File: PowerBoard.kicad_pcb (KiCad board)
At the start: 4 copper layers, 100 x 100 mm, 30 parts, among them U1 LT8342RV-TRMPBF, U11 PINA745AIRELR, U2 AD5259BRMZ100

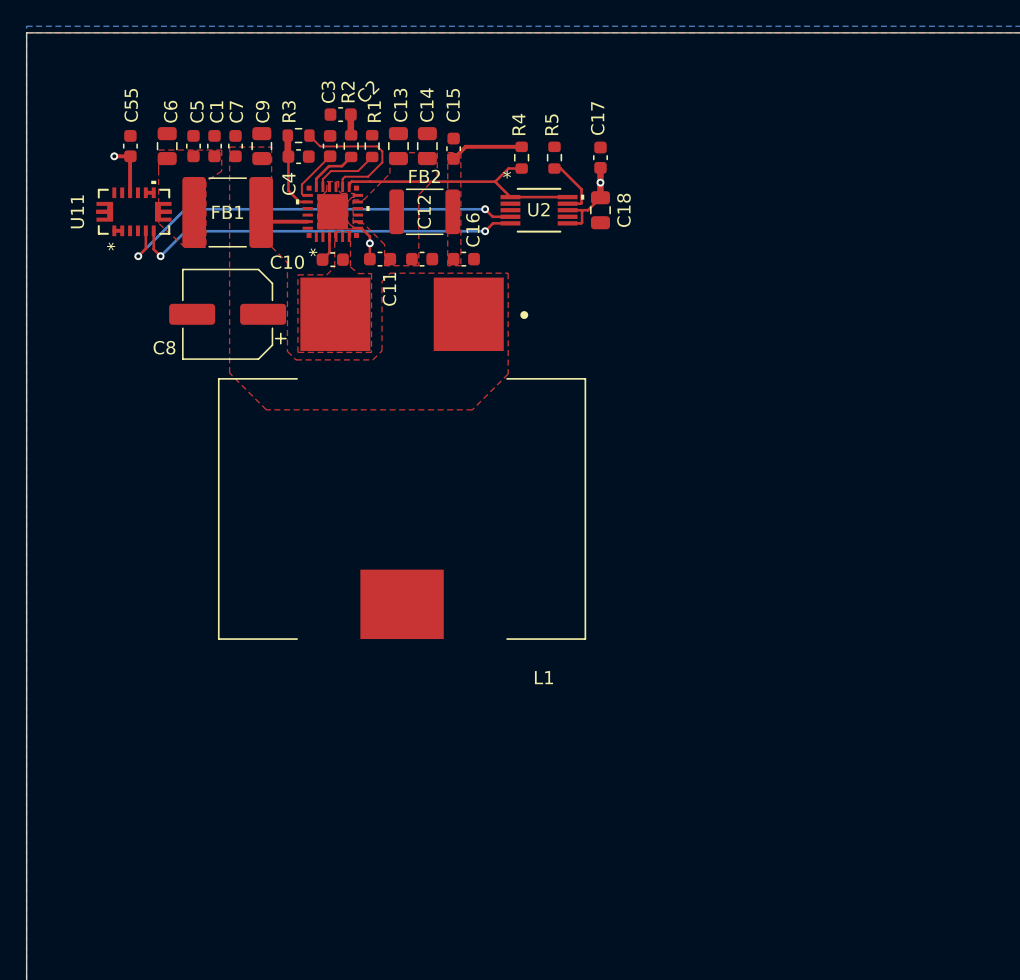
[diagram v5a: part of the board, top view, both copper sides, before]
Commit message: Most of frontend layout done. Still need to add in power and analog ground
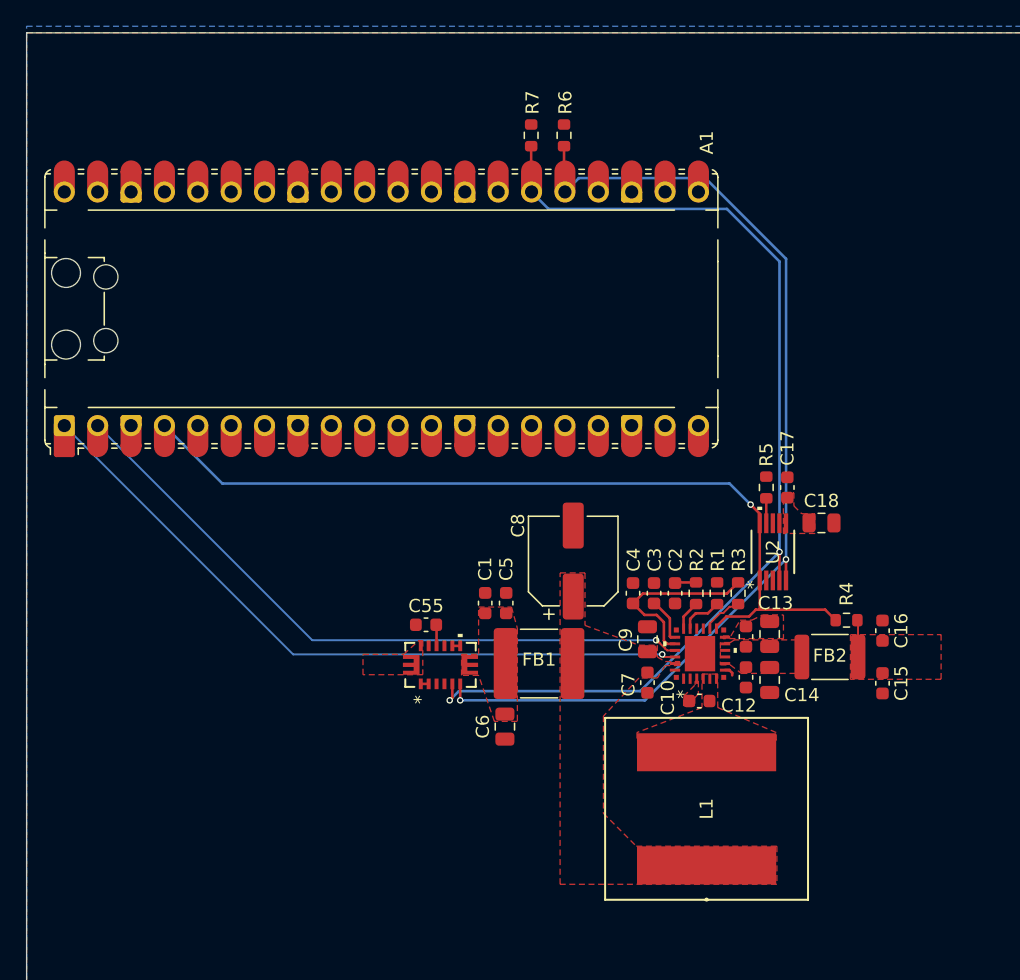
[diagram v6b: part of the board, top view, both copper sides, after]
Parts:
- added A1: RaspberryPi_Pico, Module:RaspberryPi_Pico_Common_Unspecified, F.Cu at (122.0, 65.5)
- added R6: 33k, Resistor_SMD:R_0603_1608Metric, F.Cu at (133.4, 52.3)
- added R7: 33k, Resistor_SMD:R_0603_1608Metric, F.Cu at (135.9, 52.3)
- L1: footprint _PowerBoard:IND_SER2918H-333KL -> _PowerBoard:IND_XGL1313_COC
- moved C15 52.2 mm to (160.1, 94.0), turned to -90 degrees
- moved C7 51.5 mm to (142.2, 94.0), turned to 90 degrees
- moved C6 51.1 mm to (131.4, 97.3), turned to 90 degrees
- moved R3 48.3 mm to (149.2, 87.2), turned to -90 degrees
- moved C14 48.3 mm to (151.6, 93.8), turned to 90 degrees
- moved C9 47.6 mm to (142.2, 90.7)
- moved C13 46.7 mm to (151.6, 90.2)
- moved FB2 45.8 mm to (156.1, 92.0)
- moved C2 44.4 mm to (144.3, 87.2), turned to 90 degrees
- moved U1 43.7 mm to (146.2, 91.8)
- moved C10 43.7 mm to (146.2, 95.3)
- moved R4 43.0 mm to (157.4, 89.2), turned to 0 degrees
- moved R1 43.0 mm to (147.6, 87.2)
- moved R2 43.0 mm to (145.9, 87.2)
- moved C55 42.8 mm to (125.4, 89.5), turned to 0 degrees
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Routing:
- net /Main/SX_B.EN: track 0.00 -> 53.8 mm, vias 0 -> 1
- net /Main/SX_B.PGOOD: track 0.00 -> 51.0 mm, vias 0 -> 1
- net /Main/SCL: track 29.7 -> 77.6 mm
- net /Main/SDA: track 32.2 -> 79.2 mm
- net /Main/SX_B.FB: track 20.5 -> 65.5 mm, vias 0 -> 1
- net +5V: track 11.2 -> 1.76 mm, vias 2 -> 0
- net Net-(U1-VSET1): track 11.0 -> 3.08 mm
- net /Main/boost_a_frontend/INTVCC: track 6.04 -> 14.0 mm
- net Net-(U1-VIN): track 3.83 -> 0.00 mm
- net Net-(U2-B): track 4.84 -> 1.90 mm
- net /Main/boost_a_control/VOUT_IN: track 5.56 -> 2.82 mm
- net Net-(U1-BST): track 1.95 -> 0.00 mm
- net Net-(U1-RT): track 5.03 -> 3.26 mm
- net GND: track 2.89 -> 1.17 mm, vias 1 -> 0
- net Net-(U1-VC): track 3.95 -> 2.26 mm
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- added copper zone on F.Cu, net +5V
- added copper zone on F.Cu, net /Main/boost_a_in_sns/IN
- added copper zone on F.Cu, net Net-(U1-BST)

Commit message: Working on frontend layout
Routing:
- net +5V: track 1.76 -> 6.75 mm, vias 0 -> 5
- net /Main/SCL: track 77.6 -> 80.7 mm
- net /Main/SDA: track 79.2 -> 81.6 mm
- net GND: track 1.17 -> 2.24 mm, vias 0 -> 40

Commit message: Finished with layout
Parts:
- added TP1: PANEL_A_DRV_TP, MountingHole:MountingHole_6mm_Pad_TopBottom, F.Cu at (113.0, 92.5)
- added TP10: SX_BOOST_PGOOD, MountingHole:MountingHole_6mm_Pad_TopBottom, F.Cu at (127.0, 130.0)
- added TP12: TestPoint, MountingHole:MountingHole_6mm_Pad_TopBottom, F.Cu at (176.0, 92.0)
- added TP2: PANEL_A_RTN_TP, MountingHole:MountingHole_6mm_Pad_TopBottom, F.Cu at (113.0, 110.0)
- added TP2: PANEL_A_RTN_TP, MountingHole:MountingHole_6mm_Pad_TopBottom, F.Cu at (176.0, 110.0)
- added TP7: BOOST_FB_TP, MountingHole:MountingHole_6mm_Pad_TopBottom, F.Cu at (166.5, 130.0)
- added TP9: SX_BOOST_EN, MountingHole:MountingHole_6mm_Pad_TopBottom, F.Cu at (147.0, 130.0)
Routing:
- net /Main/SX_B.EN: track 53.8 -> 135.3 mm
- net /Main/SX_B.PGOOD: track 51.0 -> 123.1 mm, vias 1 -> 2
- net /Main/SX_B.FB: track 65.5 -> 111.5 mm, vias 1 -> 2
